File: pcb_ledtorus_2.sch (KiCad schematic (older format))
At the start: 16 parts, among them P1 CONN_02X04, P2 CONN_6, P3 MICRO-SD, P6 CONN_12, U1 STM32F46X_LQFP176, U2 US4881_HALL

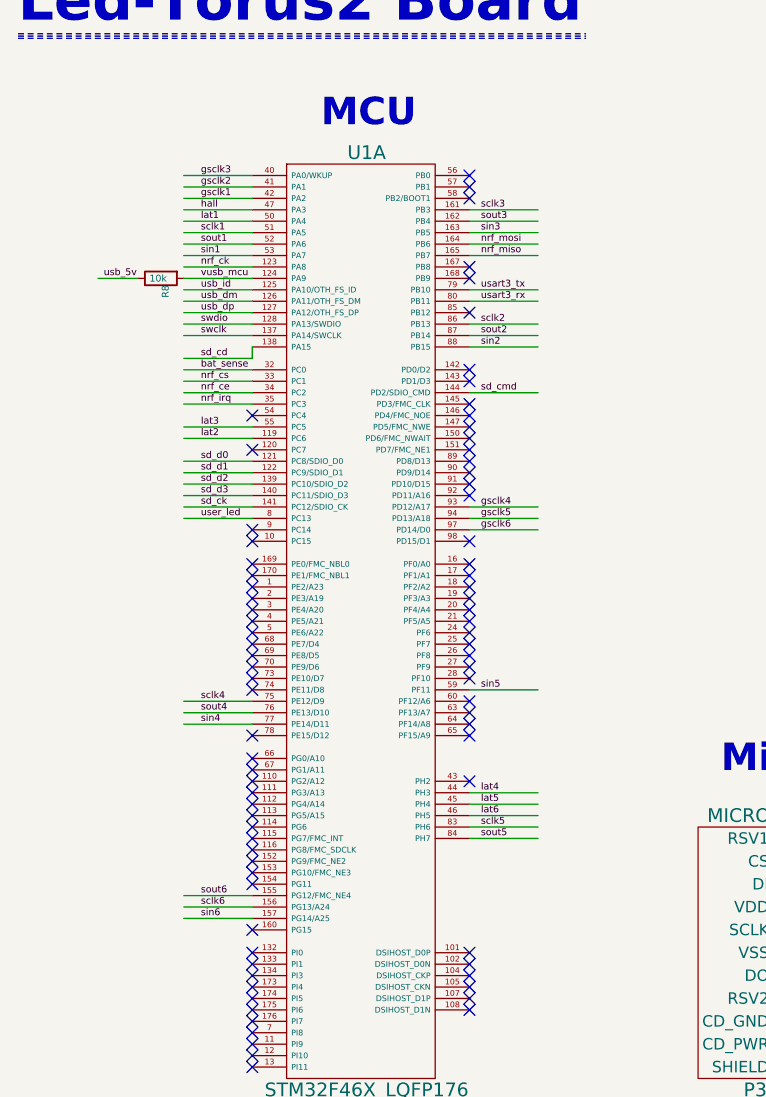
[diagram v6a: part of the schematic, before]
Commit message: Some preliminary routing of signals between TLCs and MCU.
Mostly to check that everything looks reasonably possible.
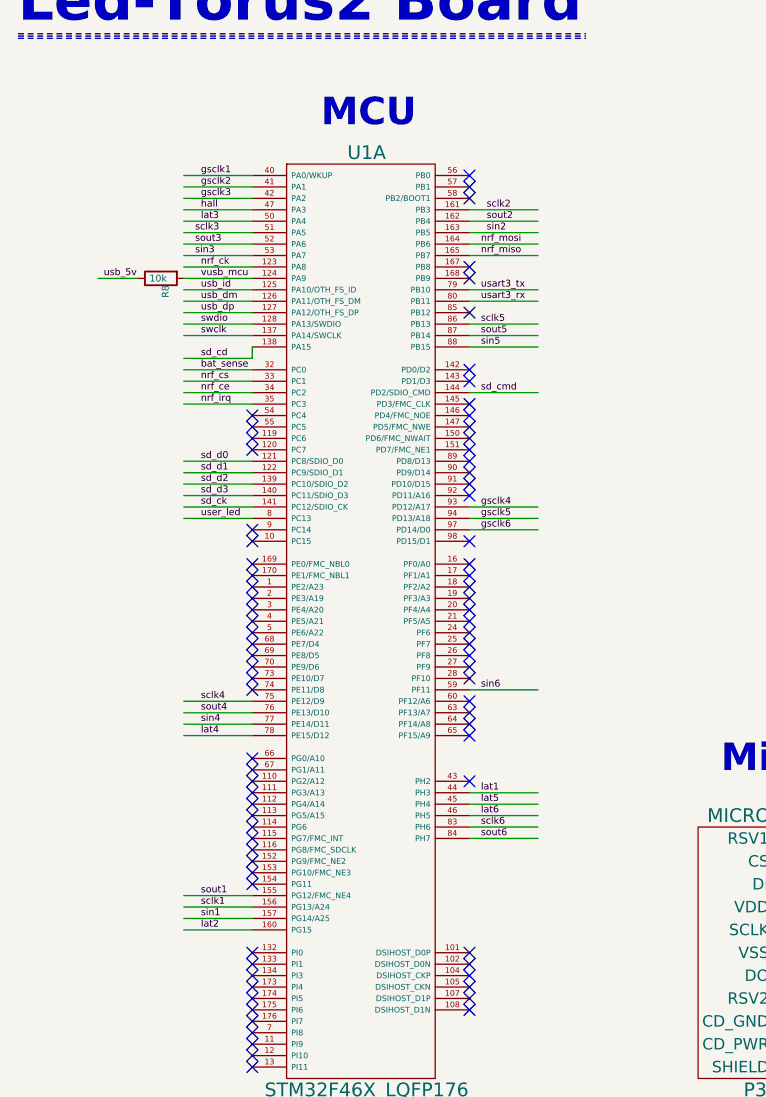
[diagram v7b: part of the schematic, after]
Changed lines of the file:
@@
 	1650 1650 1350 1650
 Wire Wire Line
-	1650 1700 1350 1700
-Wire Wire Line
-	1650 1750 1350 1750
+	2900 1600 2600 1600
+Wire Wire Line
+	2900 1650 2600 1650
 Wire Wire Line
 	1650 1800 1350 1800
@@
 	1650 2450 1350 2450
 Wire Wire Line
-	1650 2550 1350 2550
-Wire Wire Line
-	1650 2600 1350 2600
+	1650 3900 1350 3900
+Wire Wire Line
+	1650 4750 1350 4750
 Wire Wire Line
 	1650 2700 1350 2700
@@
 	1650 2250 1350 2250
 Wire Wire Line
-	2600 1600 2900 1600
-Wire Wire Line
-	2600 1650 2900 1650
+	1350 1700 1650 1700
+Wire Wire Line
+	1350 1750 1650 1750
 Wire Wire Line
 	2600 1700 2900 1700
@@
 Wire Wire Line
 	2600 2400 2900 2400
-Text Label 1425 1450 0    30   ~ 0
+Text Label 1425 1550 0    30   ~ 0
 gsclk3
 Text Label 1425 1500 0    30   ~ 0
 gsclk2
-Text Label 1425 1550 0    30   ~ 0
+Text Label 1425 1450 0    30   ~ 0
 gsclk1
 Text Label 1425 1600 0    30   ~ 0
 hall
-Text Label 1425 1700 0    30   ~ 0
-sclk1
-Text Label 1425 1750 0    30   ~ 0
-sout1
-Text Label 1425 1800 0    30   ~ 0
-sin1
-Text Label 2650 1600 0    30   ~ 0
+Text Label 2675 1600 0    30   ~ 0
+sclk2
+Text Label 2675 1650 0    30   ~ 0
+sout2
+Text Label 2675 1700 0    30   ~ 0
+sin2
+Text Label 1400 1700 0    30   ~ 0
 sclk3
-Text Label 2650 1650 0    30   ~ 0
+Text Label 1400 1750 0    30   ~ 0
 sout3
-Text Label 2650 1700 0    30   ~ 0
+Text Label 1400 1800 0    30   ~ 0
 sin3
 Text Label 2650 2150 0    30   ~ 0
-sout2
+sout5
 Text Label 2650 2200 0    30   ~ 0
-sin2
+sin5
 Text Label 2650 2100 0    30   ~ 0
-sclk2
+sclk5
 Text Label 1425 2800 0    30   ~ 0
 sd_d2
@@
 Text Label 1425 2450 0    30   ~ 0
 nrf_irq
-Text Label 1425 2550 0    30   ~ 0
-lat3
-Text Label 1425 2600 0    30   ~ 0
+Text Label 1425 3900 0    30   ~ 0
+lat4
+Text Label 1425 4750 0    30   ~ 0
 lat2
 Text Label 1425 2950 0    30   ~ 0
@@
 usart3_rx
 Text Label 1425 1650 0    30   ~ 0
-lat1
+lat3
 NoConn ~ 2600 1550
 NoConn ~ 2600 2050
@@
 sin4
 Text Label 1425 4600 0    30   ~ 0
-sout6
+sout1
 Text Label 1425 4650 0    30   ~ 0
-sclk6
+sclk1
 Text Label 1425 4700 0    30   ~ 0
-sin6
+sin1
 Wire Wire Line
 	2600 3700 2900 3700
 Text Label 2650 3700 0    30   ~ 0
-sin5
+sin6
 Text Label 2650 4300 0    30   ~ 0
-sclk5
+sclk6
 Text Label 2650 4350 0    30   ~ 0
-sout5
+sout6
 Wire Wire Line
 	2600 4300 2900 4300
@@
 NoConn ~ 2600 3850
 NoConn ~ 2600 3900
-NoConn ~ 1650 3900
+NoConn ~ 1650 2550
 NoConn ~ 1650 4000
 NoConn ~ 1650 4050
@@
 NoConn ~ 1650 5300
 NoConn ~ 1650 5350
-NoConn ~ 1650 4750
+NoConn ~ 1650 2600
 NoConn ~ 2600 3050
 $Comp
@@
 	2600 4250 2900 4250
 Text Label 2650 4150 0    30   ~ 0
-lat4
+lat1
 Text Label 2650 4200 0    30   ~ 0
 lat5

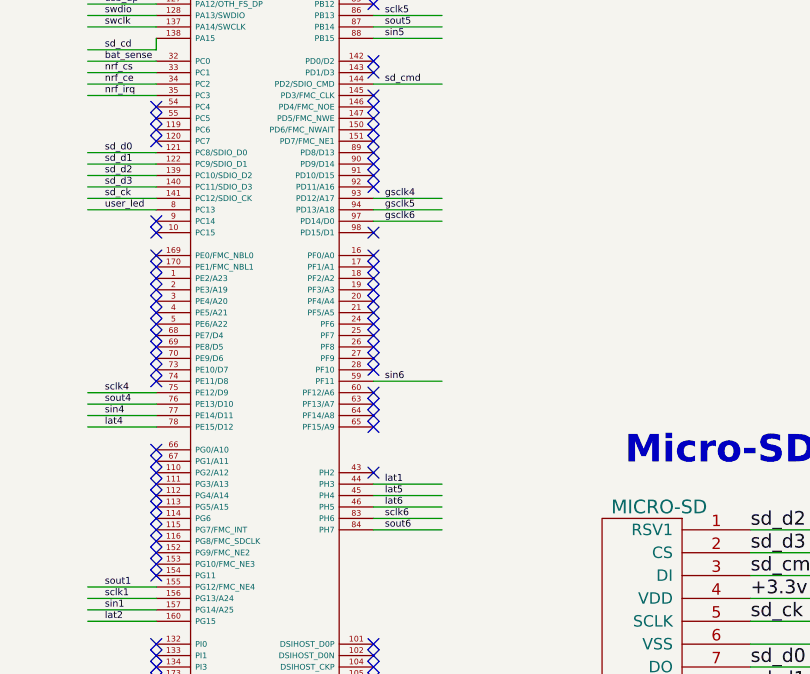
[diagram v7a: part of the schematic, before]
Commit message: Back TLC part of lower half of LEDs routed.
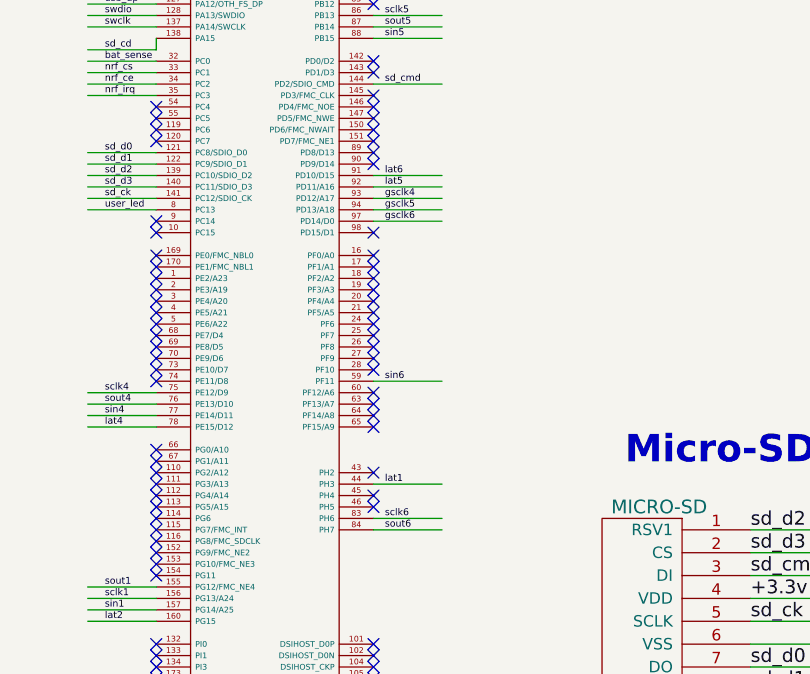
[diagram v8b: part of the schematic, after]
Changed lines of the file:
@@
 	1    0    0    -1
 $EndComp
-NoConn ~ 2600 2850
-NoConn ~ 2600 2800
+NoConn ~ 2600 4250
+NoConn ~ 2600 4200
 NoConn ~ 2600 2750
 Wire Wire Line
 	2600 4150 2900 4150
 Wire Wire Line
-	2600 4200 2900 4200
+	2600 2800 2900 2800
 Wire Wire Line
-	2600 4250 2900 4250
+	2600 2850 2900 2850
 Text Label 2650 4150 0    30   ~ 0
 lat1
-Text Label 2650 4200 0    30   ~ 0
+Text Label 2650 2850 0    30   ~ 0
 lat5
-Text Label 2650 4250 0    30   ~ 0
+Text Label 2650 2800 0    30   ~ 0
 lat6
 $Comp
